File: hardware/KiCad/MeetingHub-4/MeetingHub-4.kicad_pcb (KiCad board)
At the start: 2 copper layers, 118 x 123 mm, 70 parts, among them J1 USB-C POWER IN, J2 TRRS Notebook 1, J3 TRRS Notebook 2, J4 TRRS Notebook 3, J5 TRRS Notebook 4, J6 Headset (User), K1 Select NB1, K2 Select NB2, K3 Select NB3, K4 Select NB4, SW1 MUTE, SW2 Select NB1, SW3 Select NB2, SW4 Select NB3, SW5 Select NB4, U1 NE5532, U2 NJM4556A

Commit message: Update PCB-001 guide: front/top/back panel arrangement, applied layout
Replaces the generic panel-component table and schematic-sheet-based
zoning diagram with the arrangement actually decided and applied: J6 +
mic mute/select switches on the front (most frequently touched), volume
pots on top, notebook TRRS jacks + USB-C + power at the back (plugged
once, rarely touched). Fase 4 now documents the applied result instead of
a future to-do, with a note that spacing was validated by anchor-distance
only and still needs a visual/physical check.

Co-Authored-By: Claude Sonnet 5 <noreply@anthropic.com>
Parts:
- moved RV5 1137.1 mm to (270.0, 170.0)
- moved D1 1123.3 mm to (310.0, 120.0)
- moved C2 1112.7 mm to (310.0, 135.0)
- moved F1 1101.5 mm to (290.0, 120.0)
- moved RV4 1100.8 mm to (230.0, 170.0)
- moved J1 1096.9 mm to (290.0, 100.0)
- moved R15 1093.5 mm to (251.0, 182.0)
- moved R19 1092.4 mm to (251.0, 193.0)
- moved C1 1092.3 mm to (290.0, 135.0)
- moved SW5 1091.4 mm to (200.0, 218.0)
- moved C17 1085.4 mm to (251.0, 204.0)
- moved R14 1082.7 mm to (239.0, 182.0)
- moved R18 1081.5 mm to (239.0, 193.0)
- moved SW4 1078.7 mm to (185.0, 218.0)
- moved C21 1076.9 mm to (251.0, 215.0)
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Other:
- board size 118 x 123 mm -> 265 x 160 mm

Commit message: Align front (J6+SW1-5) and back (P2+USB-C) panel rows
Both rows were on the correct edge already but at slightly different Y
per component; now every connector in each row shares the same Y with
uniform pitch, matching a real front-panel/back-panel strip. Power
cluster (F1, D1, C1, C2, TP1) shifted along with J1 to stay adjacent.

Co-Authored-By: Claude Sonnet 5 <noreply@anthropic.com>
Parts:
- moved J6 40.0 mm to (230.0, 232.0)
- moved C1 20.0 mm to (270.0, 135.0)
- moved C2 20.0 mm to (290.0, 135.0)
- moved D1 20.0 mm to (290.0, 120.0)
- moved F1 20.0 mm to (270.0, 120.0)
- moved J1 20.0 mm to (270.0, 100.0)
- moved TP1 20.0 mm to (250.0, 120.0)
- moved SW5 18.4 mm to (212.0, 232.0)
- moved SW4 16.6 mm to (194.0, 232.0)
- moved SW3 15.2 mm to (176.0, 232.0)
- moved SW2 14.3 mm to (158.0, 232.0)
- moved SW1 14.0 mm to (140.0, 232.0)
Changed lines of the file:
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@@
   )
   (footprint "Capacitor_THT:CP_Radial_D5.0mm_P2.00mm" (layer "F.Cu")
-    (at 310 135)
+    (at 290 135)
     (descr "CP, Radial series, Radial, pin pitch=2.00mm, , diameter=5mm, Electrolytic Capacitor")
     (tags "CP Radial series Radial pin pitch 2.00mm  diameter 5mm Electrolytic Capacitor")
@@
   )
   (footprint "Connector_USB:USB_C_Receptacle_GCT_USB4085" (layer "F.Cu")
-    (at 290 100)
+    (at 270 100)
     (descr "USB 2.0 Type C Receptacle, https://gct.co/Files/Drawings/USB4085.pdf")
     (tags "USB Type-C Receptacle Through-hole Right angle")
@@
   )
   (footprint "Connector_JST:JST_XH_B2B-XH-A_1x02_P2.50mm_Vertical" (layer "F.Cu")
-    (at 185 218)
+    (at 194 232)
     (descr "JST XH series connector, B2B-XH-A (http://www.jst-mfg.com/product/pdf/eng/eXH.pdf), generated with kicad-footprint-generator")
     (tags "connector JST XH vertical")
@@
   )
   (footprint "Diode_THT:D_DO-41_SOD81_P10.16mm_Horizontal" (layer "F.Cu")
-    (at 310 120)
+    (at 290 120)
     (descr "Diode, DO-41_SOD81 series, Axial, Horizontal, pin pitch=10.16mm, , length*diameter=5.2*2.7mm^2, , http://www.diodes.com/_files/packages/DO-41%20(Plastic).pdf")
     (tags "Diode DO-41_SOD81 series Axial Horizontal pin pitch 10.16mm  length 5.2mm diameter 2.7mm")
@@
   )
   (footprint "Capacitor_THT:C_Disc_D5.0mm_W2.5mm_P2.50mm" (layer "F.Cu")
-    (at 290 135)
+    (at 270 135)
     (descr "C, Disc series, Radial, pin pitch=2.50mm, , diameter*width=5*2.5mm^2, Capacitor, http://cdn-reichelt.de/documents/datenblatt/B300/DS_KERKO_TC.pdf")
     (tags "C Disc series Radial pin pitch 2.50mm  diameter 5mm width 2.5mm Capacitor")
@@
   )
   (footprint "TestPoint:TestPoint_THTPad_D1.5mm_Drill0.7mm" (layer "F.Cu")
-    (at 270 120)
+    (at 250 120)
     (descr "THT pad as test Point, diameter 1.5mm, hole diameter 0.7mm")
     (tags "test point THT pad")
@@
   )
   (footprint "Fuse:Fuse_Bourns_MF-RG500" (layer "F.Cu")
-    (at 290 120)
+    (at 270 120)
     (descr "PTC Resettable Fuse, Ihold = 5.0A, Itrip=8.5A, http://www.bourns.com/docs/Product-Datasheets/mfrg.pdf")
     (tags "ptc resettable fuse polyfuse THT")
@@
   )
   (footprint "Connector_JST:JST_XH_B2B-XH-A_1x02_P2.50mm_Vertical" (layer "F.Cu")
-    (at 140 218)
+    (at 140 232)
     (descr "JST XH series connector, B2B-XH-A (http://www.jst-mfg.com/product/pdf/eng/eXH.pdf), generated with kicad-footprint-generator")
     (tags "connector JST XH vertical")
@@
   )
   (footprint "Connector_JST:JST_XH_B2B-XH-A_1x02_P2.50mm_Vertical" (layer "F.Cu")
-    (at 170 218)
+    (at 176 232)
     (descr "JST XH series connector, B2B-XH-A (http://www.jst-mfg.com/product/pdf/eng/eXH.pdf), generated with kicad-footprint-generator")
     (tags "connector JST XH vertical")
@@
   )
   (footprint "Connector_Audio:Jack_3.5mm_PJ320D_Horizontal" (layer "F.Cu")
-    (at 190 230)
+    (at 230 232)
     (descr "Headphones with microphone connector, 3.5mm, 4 pins (http://www.qingpu-electronics.com/en/products/WQP-PJ320D-72.html)")
     (tags "3.5mm jack mic microphone phones headphones 4pins audio plug")
@@
   )
   (footprint "Connector_JST:JST_XH_B2B-XH-A_1x02_P2.50mm_Vertical" (layer "F.Cu")
-    (at 155 218)
+    (at 158 232)
     (descr "JST XH series connector, B2B-XH-A (http://www.jst-mfg.com/product/pdf/eng/eXH.pdf), generated with kicad-footprint-generator")
     (tags "connector JST XH vertical")
@@
   )
   (footprint "Connector_JST:JST_XH_B2B-XH-A_1x02_P2.50mm_Vertical" (layer "F.Cu")
-    (at 200 218)
+    (at 212 232)
     (descr "JST XH series connector, B2B-XH-A (http://www.jst-mfg.com/product/pdf/eng/eXH.pdf), generated with kicad-footprint-generator")
     (tags "connector JST XH vertical")

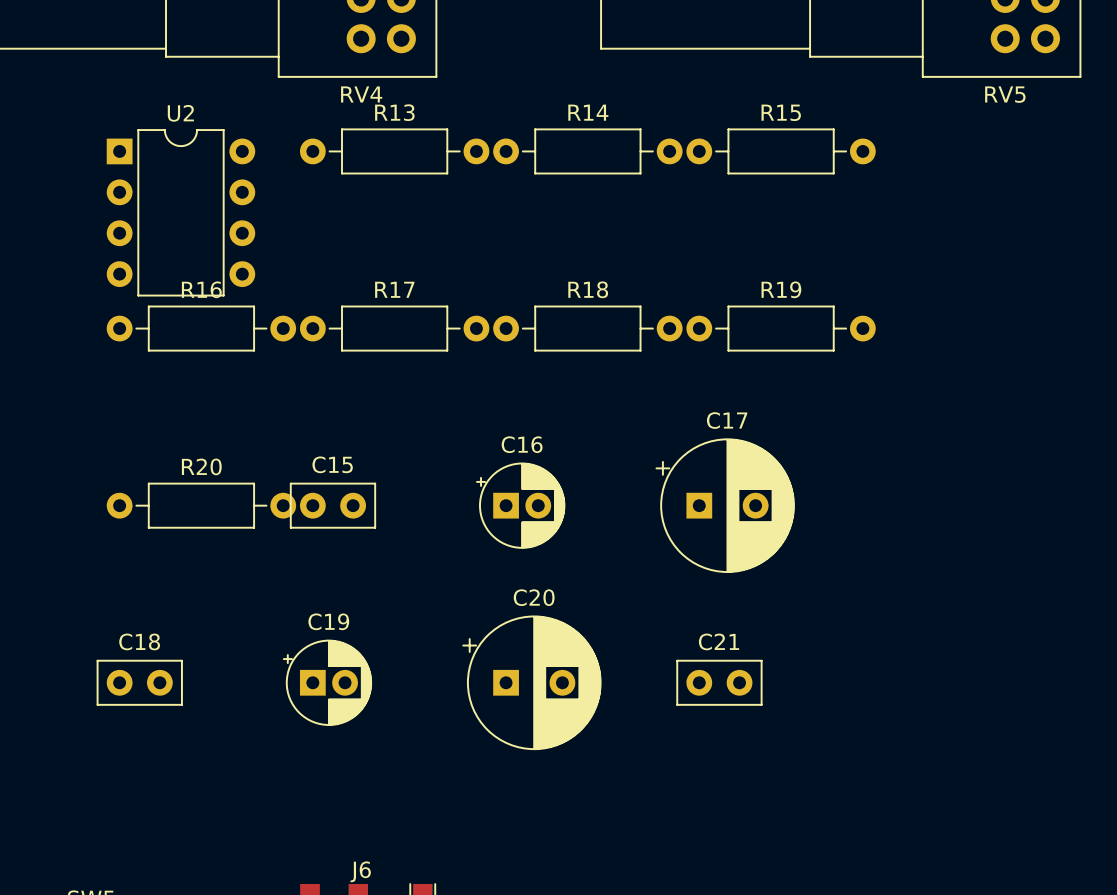
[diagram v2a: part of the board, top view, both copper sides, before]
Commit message: Fix HEADPHONE_AMP courtyard overlaps (R13-20, C15-21)
DRC flagged 6 real errors: adjacent resistors/caps in the HPAMP grid had
overlapping courtyards because the 12mm pitch was tighter than the
R_Axial_DIN0207 resistor's actual courtyard width (the MIXER grid at 13mm
pitch had zero such errors, confirming 12mm was the problem). Widened to
15mm pitch x / 12mm pitch y; board bounding box unchanged, still fits the
existing outline.

Co-Authored-By: Claude Sonnet 5 <noreply@anthropic.com>
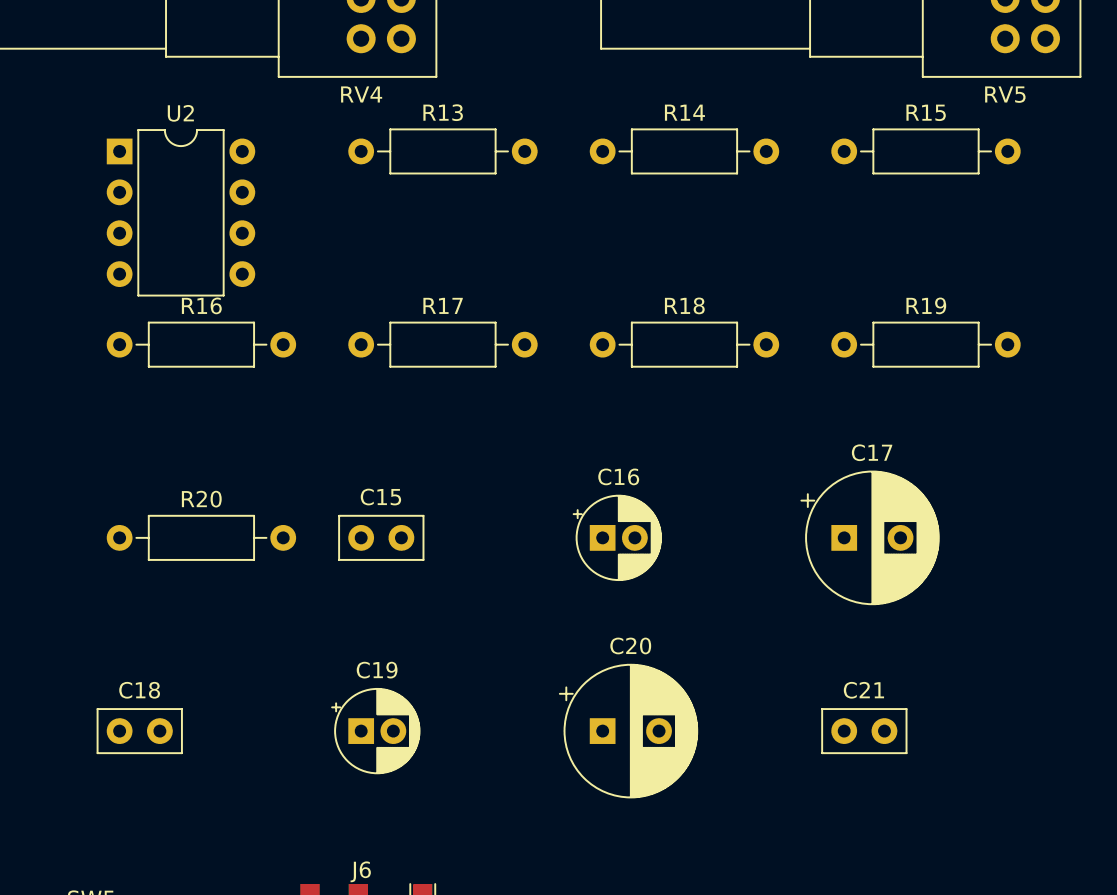
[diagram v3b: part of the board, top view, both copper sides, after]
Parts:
- moved C21 9.49 mm to (260.0, 218.0)
- moved C17 9.22 mm to (260.0, 206.0)
- moved R19 9.06 mm to (260.0, 194.0)
- moved R15 9.00 mm to (260.0, 182.0)
- moved C20 6.71 mm to (245.0, 218.0)
- moved C16 6.32 mm to (245.0, 206.0)
- moved R18 6.08 mm to (245.0, 194.0)
- moved R14 6.00 mm to (245.0, 182.0)
- moved C19 4.24 mm to (230.0, 218.0)
- moved C15 3.61 mm to (230.0, 206.0)
- moved R17 3.16 mm to (230.0, 194.0)
- moved C18 3.00 mm to (215.0, 218.0)
- moved R13 3.00 mm to (230.0, 182.0)
- moved R20 2.00 mm to (215.0, 206.0)
- moved R16 1.00 mm to (215.0, 194.0)
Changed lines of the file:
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@@
   )
   (footprint "Capacitor_THT:CP_Radial_D8.0mm_P3.50mm" (layer "F.Cu")
-    (at 251 204)
+    (at 260 206)
     (descr "CP, Radial series, Radial, pin pitch=3.50mm, , diameter=8mm, Electrolytic Capacitor")
     (tags "CP Radial series Radial pin pitch 3.50mm  diameter 8mm Electrolytic Capacitor")
@@
   )
   (footprint "Capacitor_THT:CP_Radial_D8.0mm_P3.50mm" (layer "F.Cu")
-    (at 239 215)
+    (at 245 218)
     (descr "CP, Radial series, Radial, pin pitch=3.50mm, , diameter=8mm, Electrolytic Capacitor")
     (tags "CP Radial series Radial pin pitch 3.50mm  diameter 8mm Electrolytic Capacitor")
@@
   )
   (footprint "Capacitor_THT:CP_Radial_D5.0mm_P2.00mm" (layer "F.Cu")
-    (at 239 204)
+    (at 245 206)
     (descr "CP, Radial series, Radial, pin pitch=2.00mm, , diameter=5mm, Electrolytic Capacitor")
     (tags "CP Radial series Radial pin pitch 2.00mm  diameter 5mm Electrolytic Capacitor")
@@
   )
   (footprint "Resistor_THT:R_Axial_DIN0207_L6.3mm_D2.5mm_P10.16mm_Horizontal" (layer "F.Cu")
-    (at 239 182)
+    (at 245 182)
     (descr "Resistor, Axial_DIN0207 series, Axial, Horizontal, pin pitch=10.16mm, 0.25W = 1/4W, length*diameter=6.3*2.5mm^2, http://cdn-reichelt.de/documents/datenblatt/B400/1_4W%23YAG.pdf")
     (tags "Resistor Axial_DIN0207 series Axial Horizontal pin pitch 10.16mm 0.25W = 1/4W length 6.3mm diameter 2.5mm")
@@
   )
   (footprint "Resistor_THT:R_Axial_DIN0207_L6.3mm_D2.5mm_P10.16mm_Horizontal" (layer "F.Cu")
-    (at 227 182)
+    (at 230 182)
     (descr "Resistor, Axial_DIN0207 series, Axial, Horizontal, pin pitch=10.16mm, 0.25W = 1/4W, length*diameter=6.3*2.5mm^2, http://cdn-reichelt.de/documents/datenblatt/B400/1_4W%23YAG.pdf")
     (tags "Resistor Axial_DIN0207 series Axial Horizontal pin pitch 10.16mm 0.25W = 1/4W length 6.3mm diameter 2.5mm")
@@
   )
   (footprint "Resistor_THT:R_Axial_DIN0207_L6.3mm_D2.5mm_P10.16mm_Horizontal" (layer "F.Cu")
-    (at 239 193)
+    (at 245 194)
     (descr "Resistor, Axial_DIN0207 series, Axial, Horizontal, pin pitch=10.16mm, 0.25W = 1/4W, length*diameter=6.3*2.5mm^2, http://cdn-reichelt.de/documents/datenblatt/B400/1_4W%23YAG.pdf")
     (tags "Resistor Axial_DIN0207 series Axial Horizontal pin pitch 10.16mm 0.25W = 1/4W length 6.3mm diameter 2.5mm")
@@
   )
   (footprint "Resistor_THT:R_Axial_DIN0207_L6.3mm_D2.5mm_P10.16mm_Horizontal" (layer "F.Cu")
-    (at 251 193)
+    (at 260 194)
     (descr "Resistor, Axial_DIN0207 series, Axial, Horizontal, pin pitch=10.16mm, 0.25W = 1/4W, length*diameter=6.3*2.5mm^2, http://cdn-reichelt.de/documents/datenblatt/B400/1_4W%23YAG.pdf")
     (tags "Resistor Axial_DIN0207 series Axial Horizontal pin pitch 10.16mm 0.25W = 1/4W length 6.3mm diameter 2.5mm")
@@
   )
   (footprint "Capacitor_THT:CP_Radial_D5.0mm_P2.00mm" (layer "F.Cu")
-    (at 227 215)
+    (at 230 218)
     (descr "CP, Radial series, Radial, pin pitch=2.00mm, , diameter=5mm, Electrolytic Capacitor")
     (tags "CP Radial series Radial pin pitch 2.00mm  diameter 5mm Electrolytic Capacitor")
@@
   )
   (footprint "Resistor_THT:R_Axial_DIN0207_L6.3mm_D2.5mm_P10.16mm_Horizontal" (layer "F.Cu")
-    (at 251 182)
+    (at 260 182)
     (descr "Resistor, Axial_DIN0207 series, Axial, Horizontal, pin pitch=10.16mm, 0.25W = 1/4W, length*diameter=6.3*2.5mm^2, http://cdn-reichelt.de/documents/datenblatt/B400/1_4W%23YAG.pdf")
     (tags "Resistor Axial_DIN0207 series Axial Horizontal pin pitch 10.16mm 0.25W = 1/4W length 6.3mm diameter 2.5mm")
@@
   )
   (footprint "Resistor_THT:R_Axial_DIN0207_L6.3mm_D2.5mm_P10.16mm_Horizontal" (layer "F.Cu")
-    (at 227 193)
+    (at 230 194)
     (descr "Resistor, Axial_DIN0207 series, Axial, Horizontal, pin pitch=10.16mm, 0.25W = 1/4W, length*diameter=6.3*2.5mm^2, http://cdn-reichelt.de/documents/datenblatt/B400/1_4W%23YAG.pdf")
     (tags "Resistor Axial_DIN0207 series Axial Horizontal pin pitch 10.16mm 0.25W = 1/4W length 6.3mm diameter 2.5mm")
@@
   )
   (footprint "Capacitor_THT:C_Disc_D5.0mm_W2.5mm_P2.50mm" (layer "F.Cu")
-    (at 215 215)
+    (at 215 218)
     (descr "C, Disc series, Radial, pin pitch=2.50mm, , diameter*width=5*2.5mm^2, Capacitor, http://cdn-reichelt.de/documents/datenblatt/B300/DS_KERKO_TC.pdf")
     (tags "C Disc series Radial pin pitch 2.50mm  diameter 5mm width 2.5mm Capacitor")
@@
   )
   (footprint "Capacitor_THT:C_Disc_D5.0mm_W2.5mm_P2.50mm" (layer "F.Cu")
-    (at 227 204)
+    (at 230 206)
     (descr "C, Disc series, Radial, pin pitch=2.50mm, , diameter*width=5*2.5mm^2, Capacitor, http://cdn-reichelt.de/documents/datenblatt/B300/DS_KERKO_TC.pdf")
     (tags "C Disc series Radial pin pitch 2.50mm  diameter 5mm width 2.5mm Capacitor")
@@
   )
   (footprint "Resistor_THT:R_Axial_DIN0207_L6.3mm_D2.5mm_P10.16mm_Horizontal" (layer "F.Cu")
-    (at 215 193)
+    (at 215 194)
     (descr "Resistor, Axial_DIN0207 series, Axial, Horizontal, pin pitch=10.16mm, 0.25W = 1/4W, length*diameter=6.3*2.5mm^2, http://cdn-reichelt.de/documents/datenblatt/B400/1_4W%23YAG.pdf")
     (tags "Resistor Axial_DIN0207 series Axial Horizontal pin pitch 10.16mm 0.25W = 1/4W length 6.3mm diameter 2.5mm")
@@
   )
   (footprint "Capacitor_THT:C_Disc_D5.0mm_W2.5mm_P2.50mm" (layer "F.Cu")
-    (at 251 215)
+    (at 260 218)
     (descr "C, Disc series, Radial, pin pitch=2.50mm, , diameter*width=5*2.5mm^2, Capacitor, http://cdn-reichelt.de/documents/datenblatt/B300/DS_KERKO_TC.pdf")
     (tags "C Disc series Radial pin pitch 2.50mm  diameter 5mm width 2.5mm Capacitor")
@@
   )
   (footprint "Resistor_THT:R_Axial_DIN0207_L6.3mm_D2.5mm_P10.16mm_Horizontal" (layer "F.Cu")
-    (at 215 204)
+    (at 215 206)
     (descr "Resistor, Axial_DIN0207 series, Axial, Horizontal, pin pitch=10.16mm, 0.25W = 1/4W, length*diameter=6.3*2.5mm^2, http://cdn-reichelt.de/documents/datenblatt/B400/1_4W%23YAG.pdf")
     (tags "Resistor Axial_DIN0207 series Axial Horizontal pin pitch 10.16mm 0.25W = 1/4W length 6.3mm diameter 2.5mm")

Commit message: Route the board with Freerouting (all 121 nets, 0 unrouted)
Installed OpenJDK 25 + Freerouting 2.2.4 to get a real autorouter, since
kicad-cli 7.0.11 has no DRC/routing subcommands and hand-writing 143
trace connections without a way to verify shorts was too risky.

Pipeline: exported Specctra DSN via pcbnew's ExportSpecctraDSN (respects
the project's net class rules - 0.2mm clearance/width), routed with
Freerouting (-mp 15), then applied the resulting .ses to the board using
pcbnew's own PCB_TRACK/PCB_VIA API directly (KiCad's ImportSpecctraSES
turned out to require a live GUI frame and silently no-ops headlessly, so
a custom SES parser feeds pcbnew's object API instead of hand-writing
S-expressions).

Validated before replacing the real file: paren-balanced, kicad-cli
gerber export succeeds, KiCad's own connectivity engine reports 0
unconnected pads, and a custom same-layer segment-intersection check
found 0 crossings between different nets. Net GND zone fix (from the
user's own KiCad session) also included.

Co-Authored-By: Claude Sonnet 5 <noreply@anthropic.com>
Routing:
- net +5V_AUDIO: track 0.00 -> 485.5 mm, vias 0 -> 2
- net VBIAS: track 0.00 -> 279.8 mm, vias 0 -> 1
- net NB4_L: track 0.00 -> 204.0 mm, vias 0 -> 2
- net NB4_R: track 0.00 -> 179.3 mm, vias 0 -> 2
- net NB3_R: track 0.00 -> 175.6 mm, vias 0 -> 1
- net Net-(C13-Pad2): track 0.00 -> 156.8 mm
- net Net-(R11-Pad1): track 0.00 -> 155.5 mm, vias 0 -> 1
- net NB4_MIC: track 0.00 -> 151.6 mm, vias 0 -> 1
- net Net-(C14-Pad2): track 0.00 -> 146.3 mm
- net Net-(R12-Pad1): track 0.00 -> 145.0 mm, vias 0 -> 1
- net Net-(R10-Pad1): track 0.00 -> 144.9 mm, vias 0 -> 1
- net Net-(C11-Pad2): track 0.00 -> 142.8 mm
- net NB2_MIC: track 0.00 -> 140.2 mm, vias 0 -> 1
- net NB3_MIC: track 0.00 -> 136.9 mm, vias 0 -> 1
- net Net-(C12-Pad2): track 0.00 -> 132.3 mm
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- added copper zone on B.Cu, net GND
